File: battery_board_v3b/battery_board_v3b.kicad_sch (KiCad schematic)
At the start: 201 parts, among them IC2 PCT2075DP,118, IC3 RP2040_QFN56, IC4 LT3652IMSE#PBF, J1 Bypass, J10 Jetson, J11 BM04B-SRSS-TB(LF)(SN), J14 Solar, J15 FC, J16 I2C Multiplexer Breakout, J17 ISS Foot, J18 Screw_Terminal_01x02, J19 BM04B-SRSS-TB(LF)(SN), J2 Heater, J20 CAN1, J21 BM04B-SRSS-TB(LF)(SN), J22 CAN2, J23 Conn_ARM_JTAG_SWD_10, J24 USB_B_Micro, J25 Life Makes Lemonade, J26 BM04B-SRSS-TB(LF)(SN), J27 I2C0 Breakout, J3 BURN, J4 CHARGE, J5 Foot0, J6 Foot1, J7 Foot2, J8 Foot3, J9 RBF, K1 APAN3105, Q1 IRF7458, Q10 IRLML2803, Q11 NDS8434, Q2 IRF7458, Q3 MBT2222ADW1T1, Q4 MMBT2222AT, Q5 MBT2222ADW1T1, Q6 IRLML2803, Q7 IRLML2803, Q8 NDS8434, Q9 NDS8434, SW1 KMR2, SW2 KMR2, U1 R5460N208AA, U10 TLVH431 DBZ SOT-23, U11 MCP25625-E/ML, U12 INA219AxD, U13 MAX706RESA, U14 INA219AxD, U2 1049, U3 TPS54226PWPRPWP14_2P31X2P46-L, U4 1049, U5 TPS54226PWPRPWP14_2P31X2P46-L, U6 TPS7A4501DCQT, U7 ADS1015IDGS, U8 W25Q128JV, U9 AD8495, Y1 Crystal_GND24, Y2 Crystal_GND24

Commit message: Updated JST Connectors to be All One Footprint
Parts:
- J16, J20, J22: footprint Connector_JST:JST_SH_SM04B-SRSS-TB_1x04-1MP_P1.00mm_Horizontal -> Battery Board:JST_BM04B-SRSS-TB(LF)(SN)
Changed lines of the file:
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@@
 			)
 		)
-		(property "Footprint" "Connector_JST:JST_SH_SM04B-SRSS-TB_1x04-1MP_P1.00mm_Horizontal"
+		(property "Footprint" "Battery Board:JST_BM04B-SRSS-TB(LF)(SN)"
 			(at 235.3818 260.1976 0)
 			(effects
@@
 			)
 		)
-		(property "Footprint" "Connector_JST:JST_SH_SM04B-SRSS-TB_1x04-1MP_P1.00mm_Horizontal"
+		(property "Footprint" "Battery Board:JST_BM04B-SRSS-TB(LF)(SN)"
 			(at 258.5974 259.9944 0)
 			(effects
@@
 			)
 		)
-		(property "Footprint" "Connector_JST:JST_SH_SM04B-SRSS-TB_1x04-1MP_P1.00mm_Horizontal"
+		(property "Footprint" "Battery Board:JST_BM04B-SRSS-TB(LF)(SN)"
 			(at 246.38 237.49 0)
 			(effects

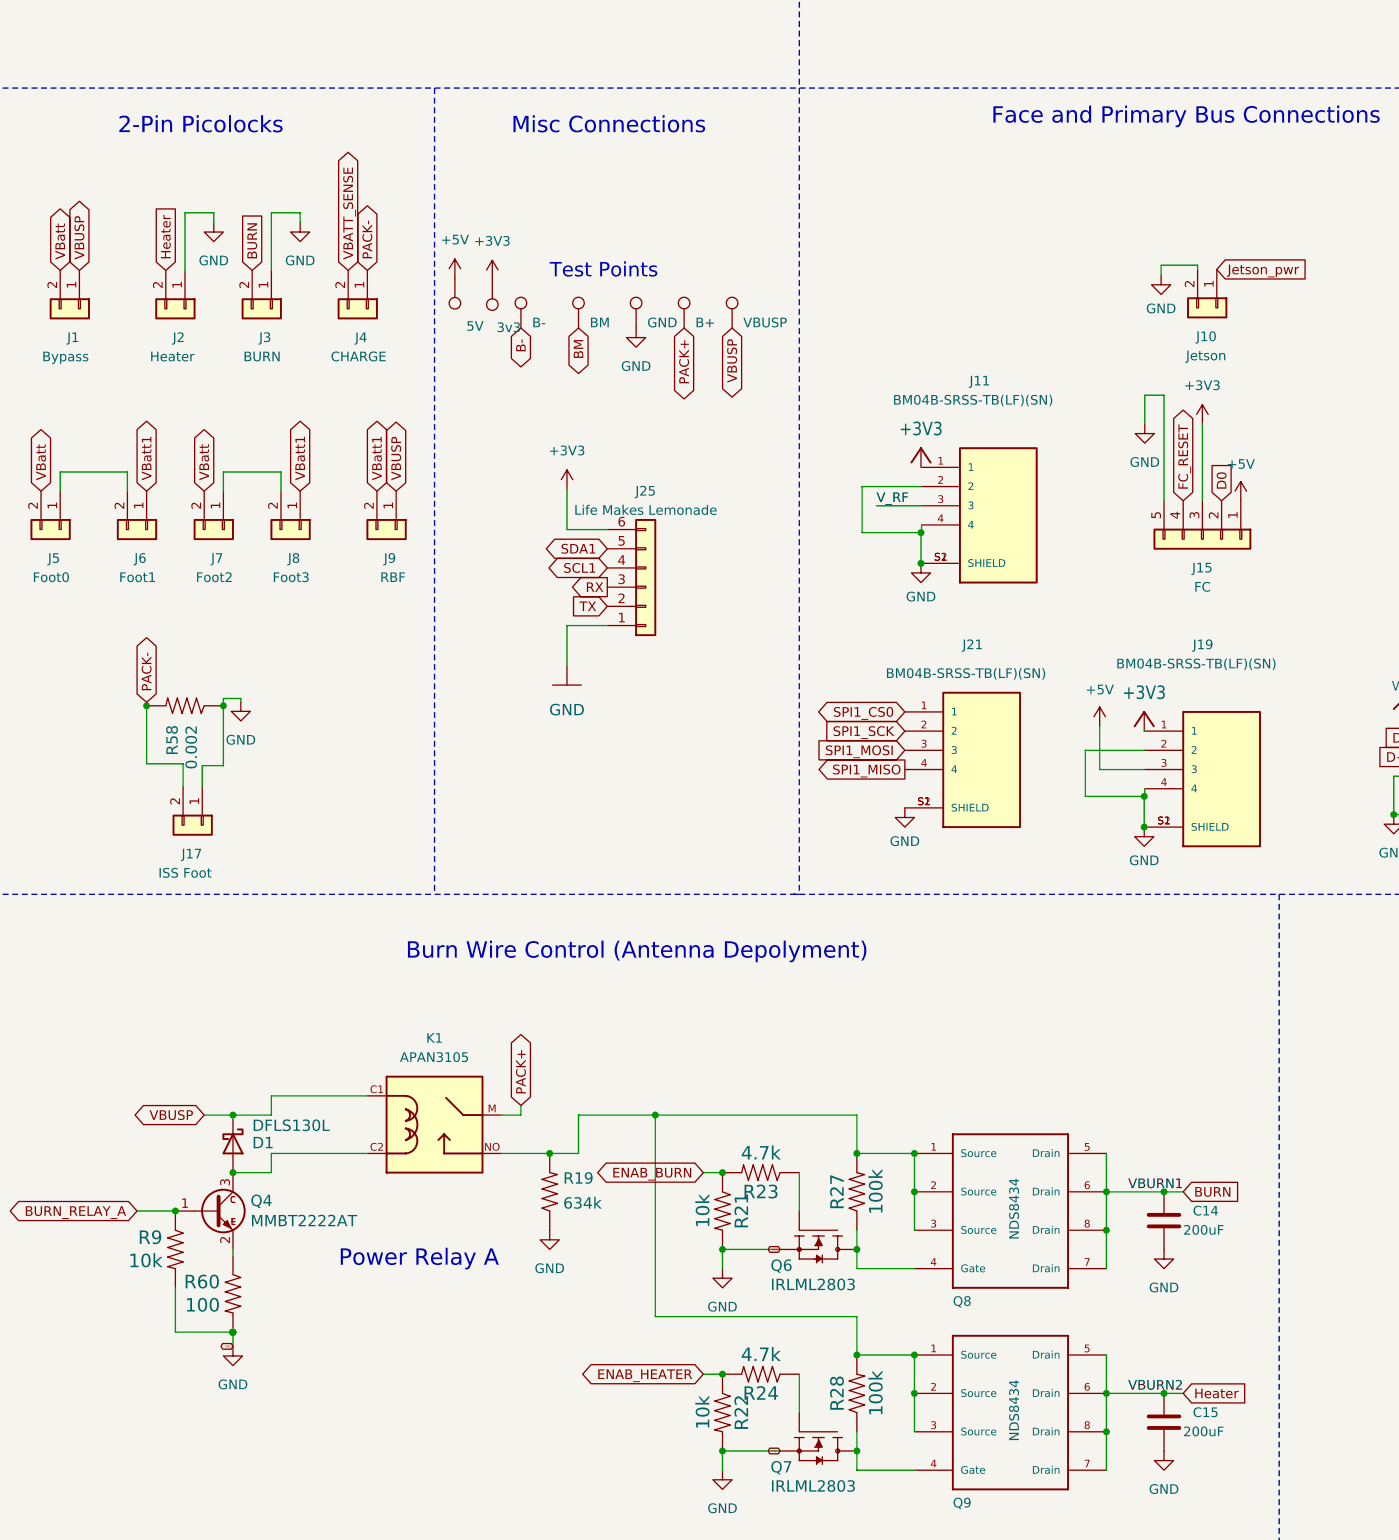
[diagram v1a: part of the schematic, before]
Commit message: Return of the 12pos Picolock
The return of the king! The 12pos picolock makes a return as a way to interface between the EPS board and the Antenna Top Cap
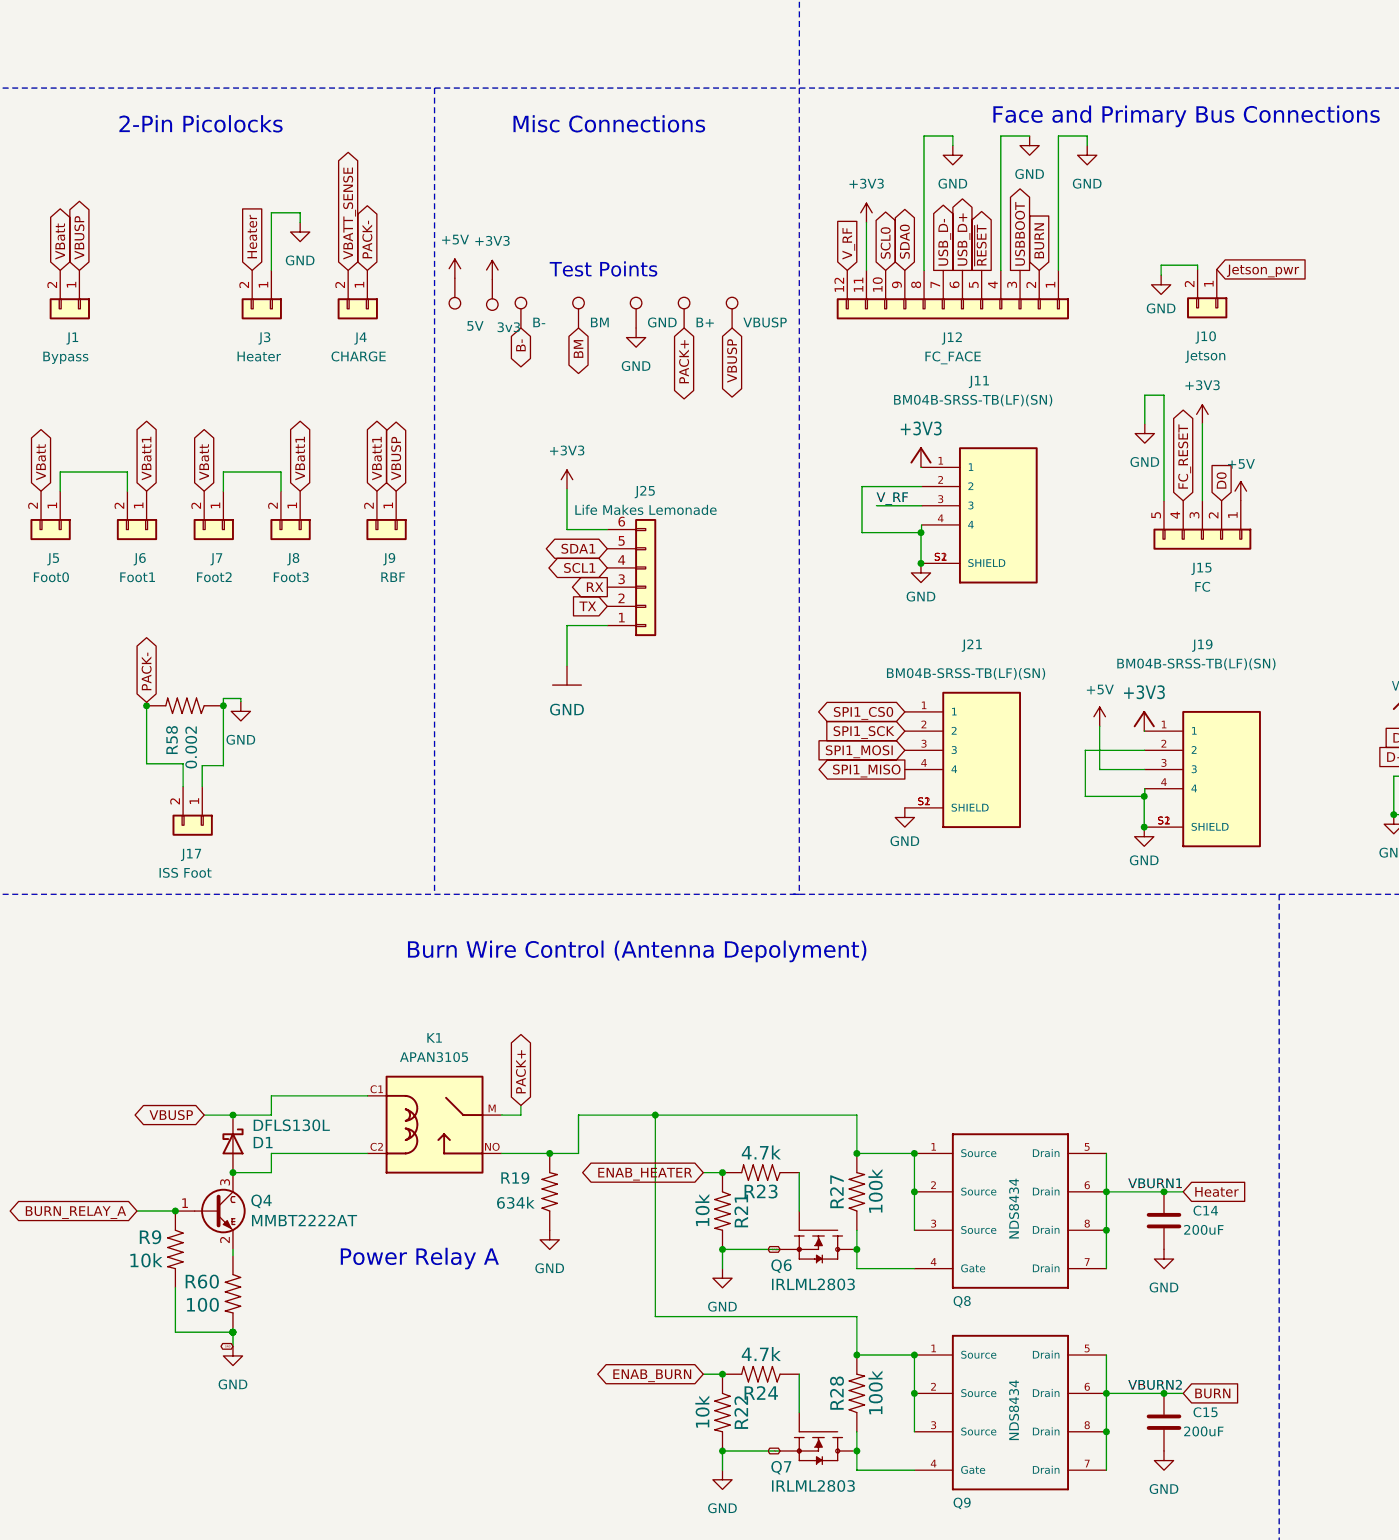
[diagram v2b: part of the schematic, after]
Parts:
- removed J2: Heater, Battery Board:MOLEX_504050-0291, symbol Connector_Generic:Conn_01x02
- added J12: FC_FACE, Connector_Molex:Molex_Pico-Lock_504050-1291_1x12-1MP_P1.50mm_Horizontal, symbol Connector_Generic:Conn_01x12
- J3: value BURN -> Heater
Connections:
- net +3V3: now also J12.11 (Pin_11)
- net BURN: now also C15.1, Q9.5 (Drain), Q9.6 (Drain), Q9.7 (Drain), Q9.8 (Drain), J12.2 (Pin_2); no longer C14.1, J3.2 (Pin_2), Q8.5 (Drain), Q8.6 (Drain), Q8.7 (Drain), Q8.8 (Drain)
- net ENAB_BURN: now also R22.1, R24.2; no longer R21.1, R23.2
- net ENAB_HEATER: now also R21.1, R23.2; no longer R22.1, R24.2
- net GND: now also J12.1 (Pin_1), J12.4 (Pin_4), J12.8 (Pin_8)
- net Heater: now also C14.1, J3.2 (Pin_2), Q8.5 (Drain), Q8.6 (Drain), Q8.7 (Drain), Q8.8 (Drain); no longer C15.1, Q9.5 (Drain), Q9.6 (Drain), Q9.7 (Drain), Q9.8 (Drain)
- net SCL0: now also J12.10 (Pin_10)
- net SDA0: now also J12.9 (Pin_9)
- net USBBOOT: now also J12.3 (Pin_3)
- net USB_D+: now also J12.6 (Pin_6)
- net USB_D-: now also J12.7 (Pin_7)
- net V_RF: now also J12.12 (Pin_12)
- net ~{RESET}: now also J12.5 (Pin_5)

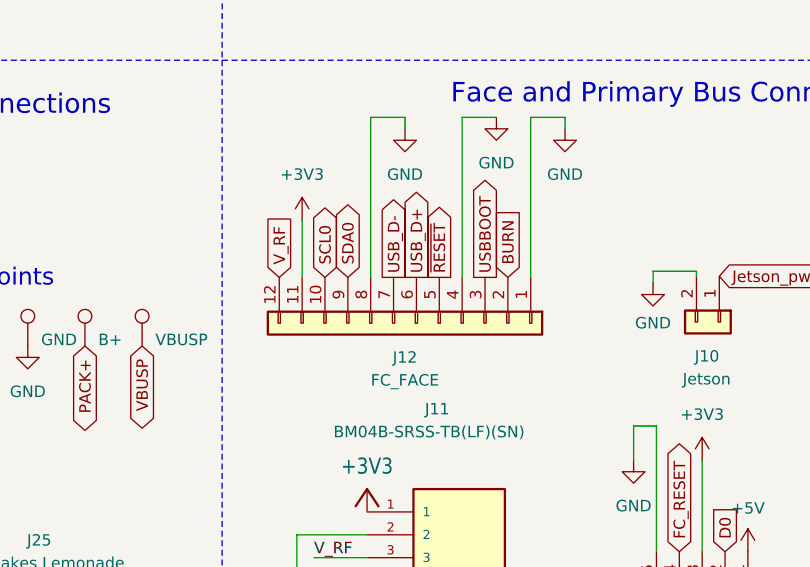
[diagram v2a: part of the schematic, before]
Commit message: Updated USB passthrough routing
Changed pass through to go through the JST conenctor
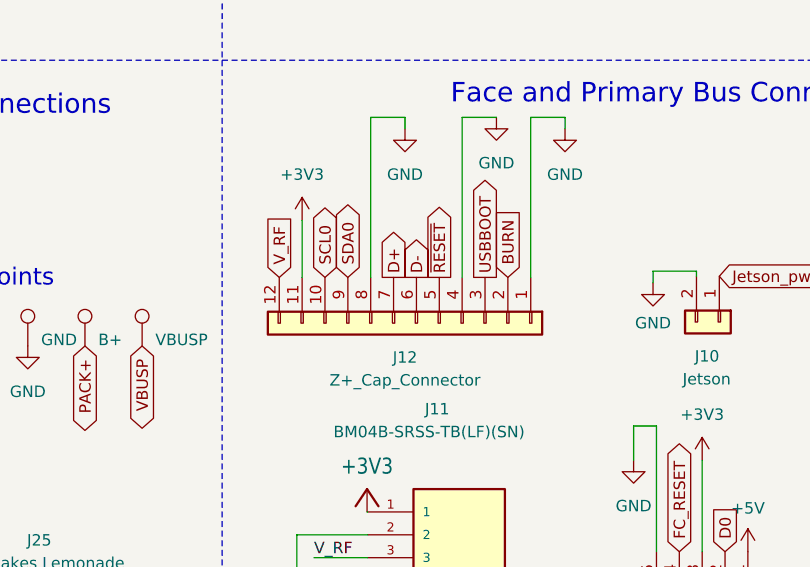
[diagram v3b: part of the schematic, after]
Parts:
- J12: value FC_FACE -> Z+_Cap_Connector
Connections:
- net D+: now also J12.7 (Pin_7)
- net D-: now also J12.6 (Pin_6)
- net USB_D+: no longer J12.6 (Pin_6)
- net USB_D-: no longer J12.7 (Pin_7)
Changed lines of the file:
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@@
 		)
 	)
+	(global_label "D+"
+		(shape output)
+		(at 137.16 227.33 90)
+		(fields_autoplaced yes)
+		(effects
+			(font
+				(size 1.27 1.27)
+			)
+			(justify left)
+		)
+		(property "Intersheetrefs" "${INTERSHEET_REFS}"
+			(at 137.16 221.5024 90)
+			(effects
+				(font
+					(size 1.27 1.27)
+				)
+				(justify left)
+				(hide yes)
+			)
+		)
+	)
 	(global_label "BURN"
 		(shape input)
@@
 		)
 	)
+	(global_label "D-"
+		(shape output)
+		(at 139.7 227.33 90)
+		(fields_autoplaced yes)
+		(effects
+			(font
+				(size 1.27 1.27)
+			)
+			(justify left)
+		)
+		(property "Intersheetrefs" "${INTERSHEET_REFS}"
+			(at 139.7 221.5024 90)
+			(effects
+				(font
+					(size 1.27 1.27)
+				)
+				(justify left)
+				(hide yes)
+			)
+		)
+	)
 	(global_label "D0"
 		(shape input)
@@
 		)
 	)
-	(global_label "USB_D+"
-		(shape output)
-		(at 139.7 227.33 90)
-		(fields_autoplaced yes)
-		(effects
-			(font
-				(size 1.27 1.27)
-			)
-			(justify left)
-		)
-		(property "Intersheetrefs" "${INTERSHEET_REFS}"
-			(at 139.7 216.7248 90)
-			(effects
-				(font
-					(size 1.27 1.27)
-				)
-				(justify left)
-				(hide yes)
-			)
-		)
-	)
 	(global_label "CHRG'"
 		(shape input)
@@
 		)
 	)
-	(global_label "USB_D-"
-		(shape output)
-		(at 137.16 227.33 90)
-		(fields_autoplaced yes)
-		(effects
-			(font
-				(size 1.27 1.27)
-			)
-			(justify left)
-		)
-		(property "Intersheetrefs" "${INTERSHEET_REFS}"
-			(at 137.16 216.7248 90)
-			(effects
-				(font
-					(size 1.27 1.27)
-				)
-				(justify left)
-				(hide yes)
-			)
-		)
-	)
 	(global_label "SPI1_MISO"
 		(shape input)
@@
 			)
 		)
-		(property "Value" "FC_FACE"
+		(property "Value" "Z+_Cap_Connector"
 			(at 138.43 238.76 90)
 			(effects

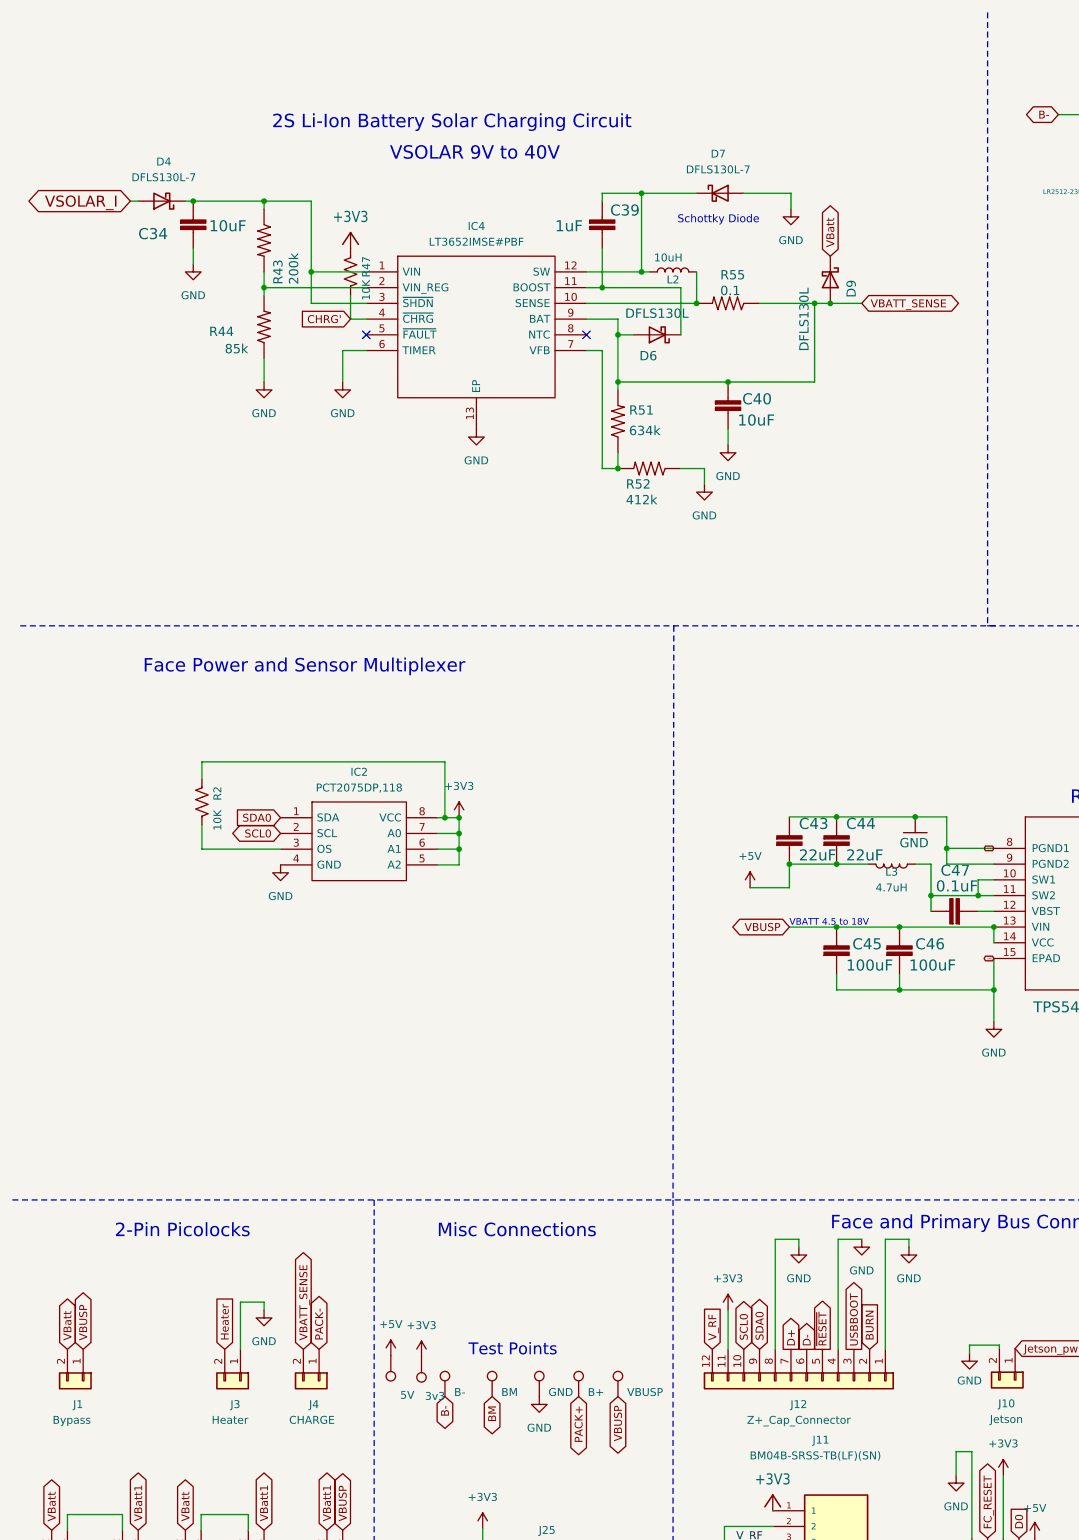
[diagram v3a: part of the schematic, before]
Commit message: As Ordered June 12, 2024
V3b finished. Recent additions:
- Direct Change Port on the 12-Pin Picolock
- Aligned charge circuit with FlatSat Dev design
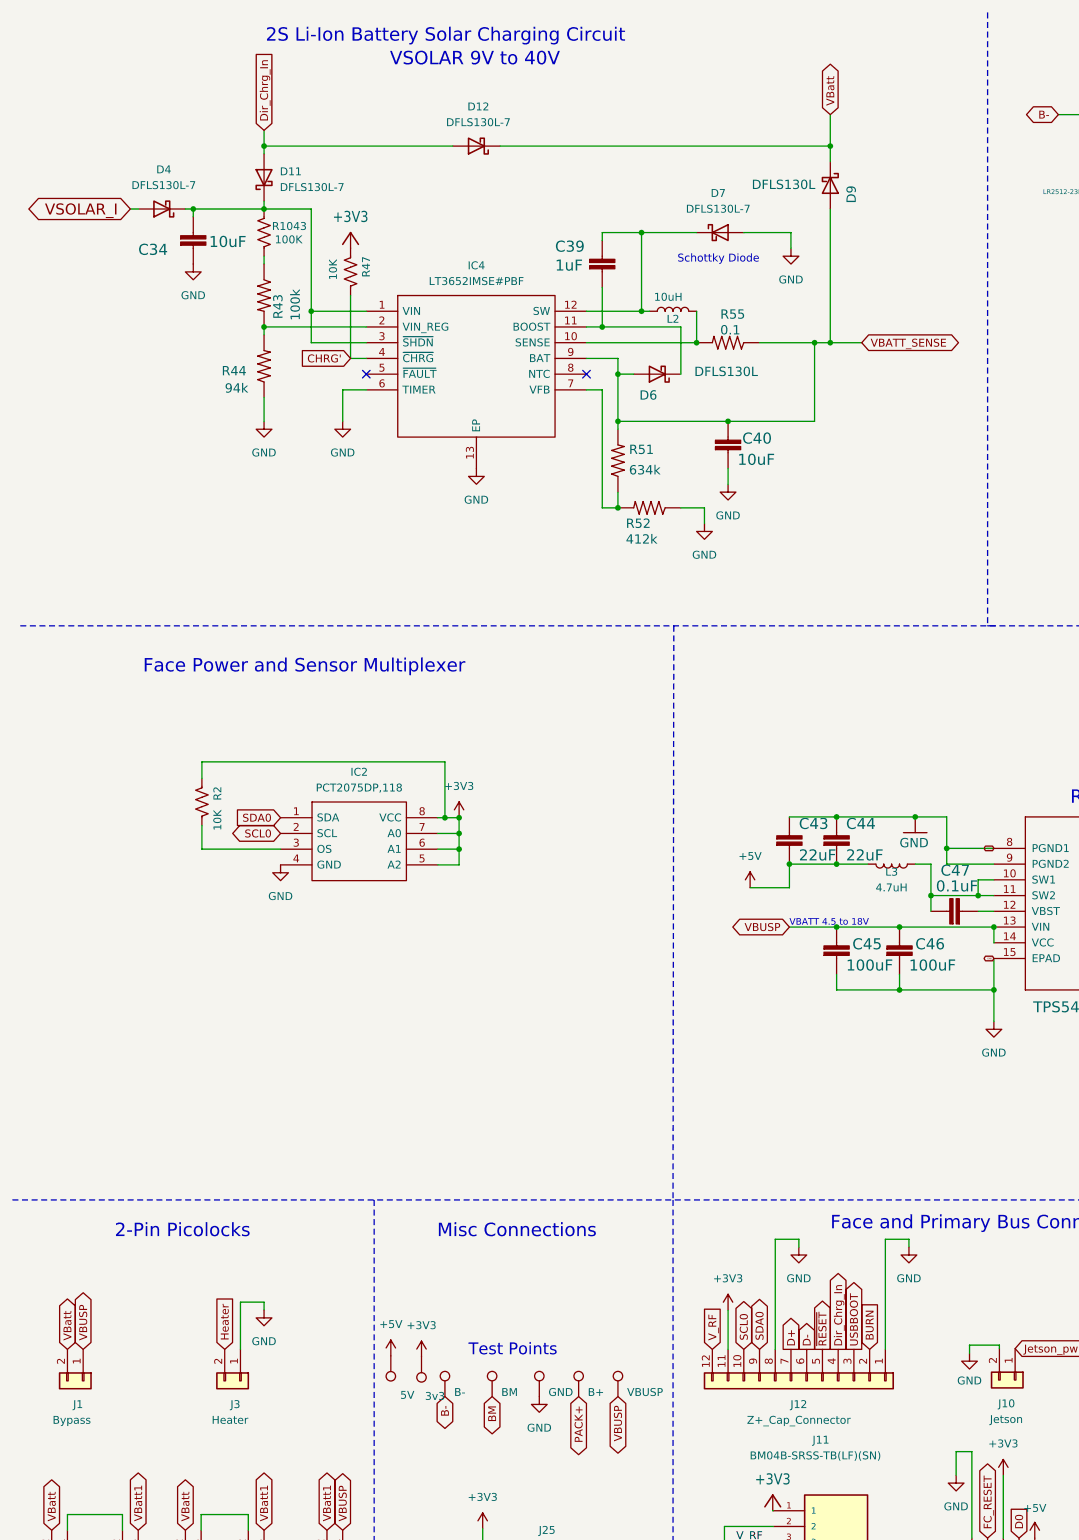
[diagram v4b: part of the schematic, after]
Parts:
- removed J4: CHARGE, Battery Board:MOLEX_504050-0291, symbol Connector_Generic:Conn_01x02
- added D11, D12: DFLS130L-7, Diode_SMD:D_PowerDI-123, symbol Device:D_Schottky
- added R1043: 100K, Resistor_SMD:R_0603_1608Metric, symbol Device:R_US
- R43: value 200k -> 100k
- R44: value 85k -> 94k
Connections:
- net GND: no longer J12.4 (Pin_4)
- net VBatt: now also D12.1 (K)
- net at C34.1, D4.1 (K), IC4.1 (VIN)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: now also D11.1 (K), R1043.1; no longer R43.1
- new net: R1043.2, R43.1
- new net Dir_Chrg_In: D11.2 (A), D12.2 (A), J12.4 (Pin_4)
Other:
- moved on the sheet: C34, C39, C40, D4, D6, D7, D9, IC4, L2, R43, R44, R51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
